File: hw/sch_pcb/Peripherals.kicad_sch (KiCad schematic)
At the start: 50 parts

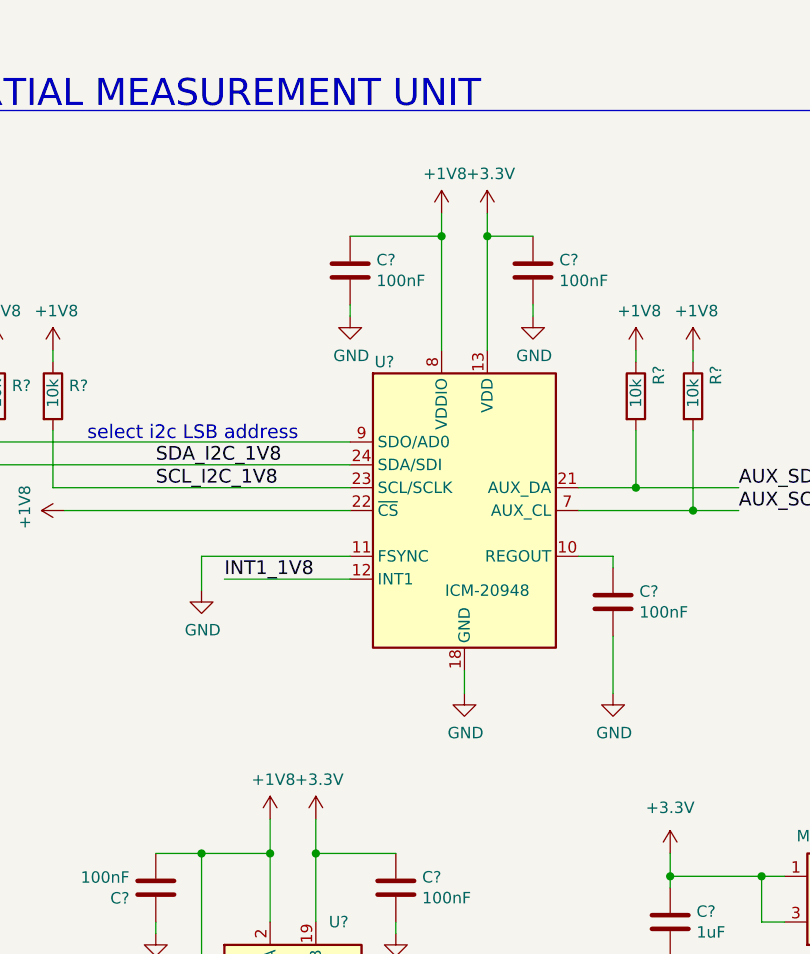
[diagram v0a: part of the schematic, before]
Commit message: Removing Li-ion accumulator BMS Adding ISM02B LoRa telemetry block.
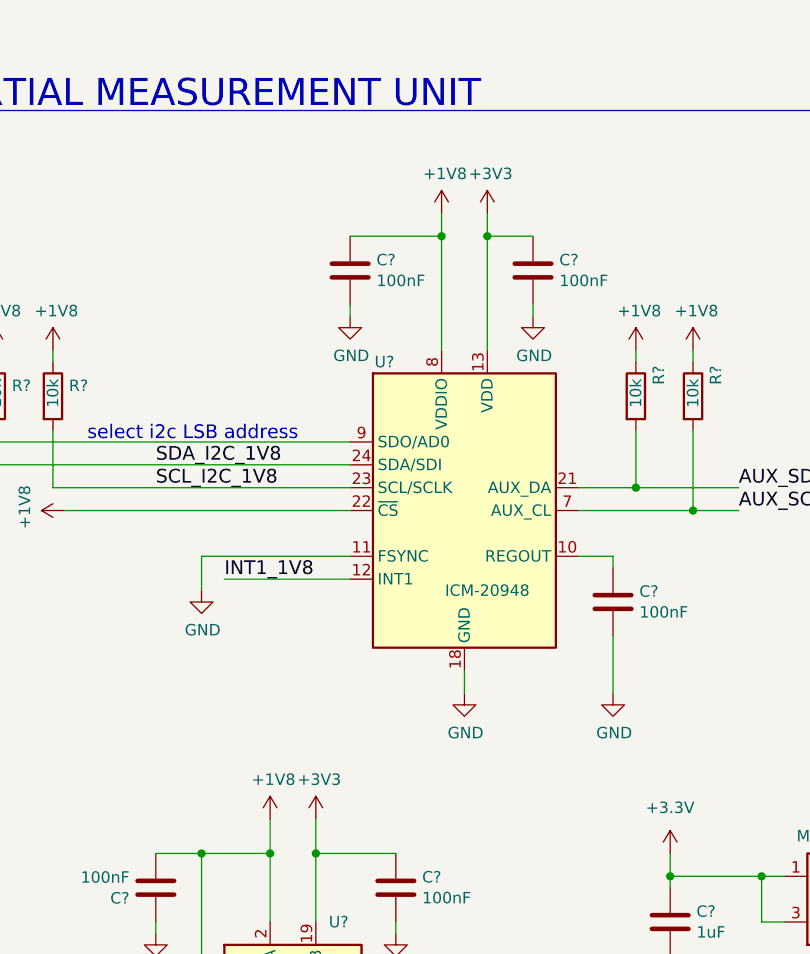
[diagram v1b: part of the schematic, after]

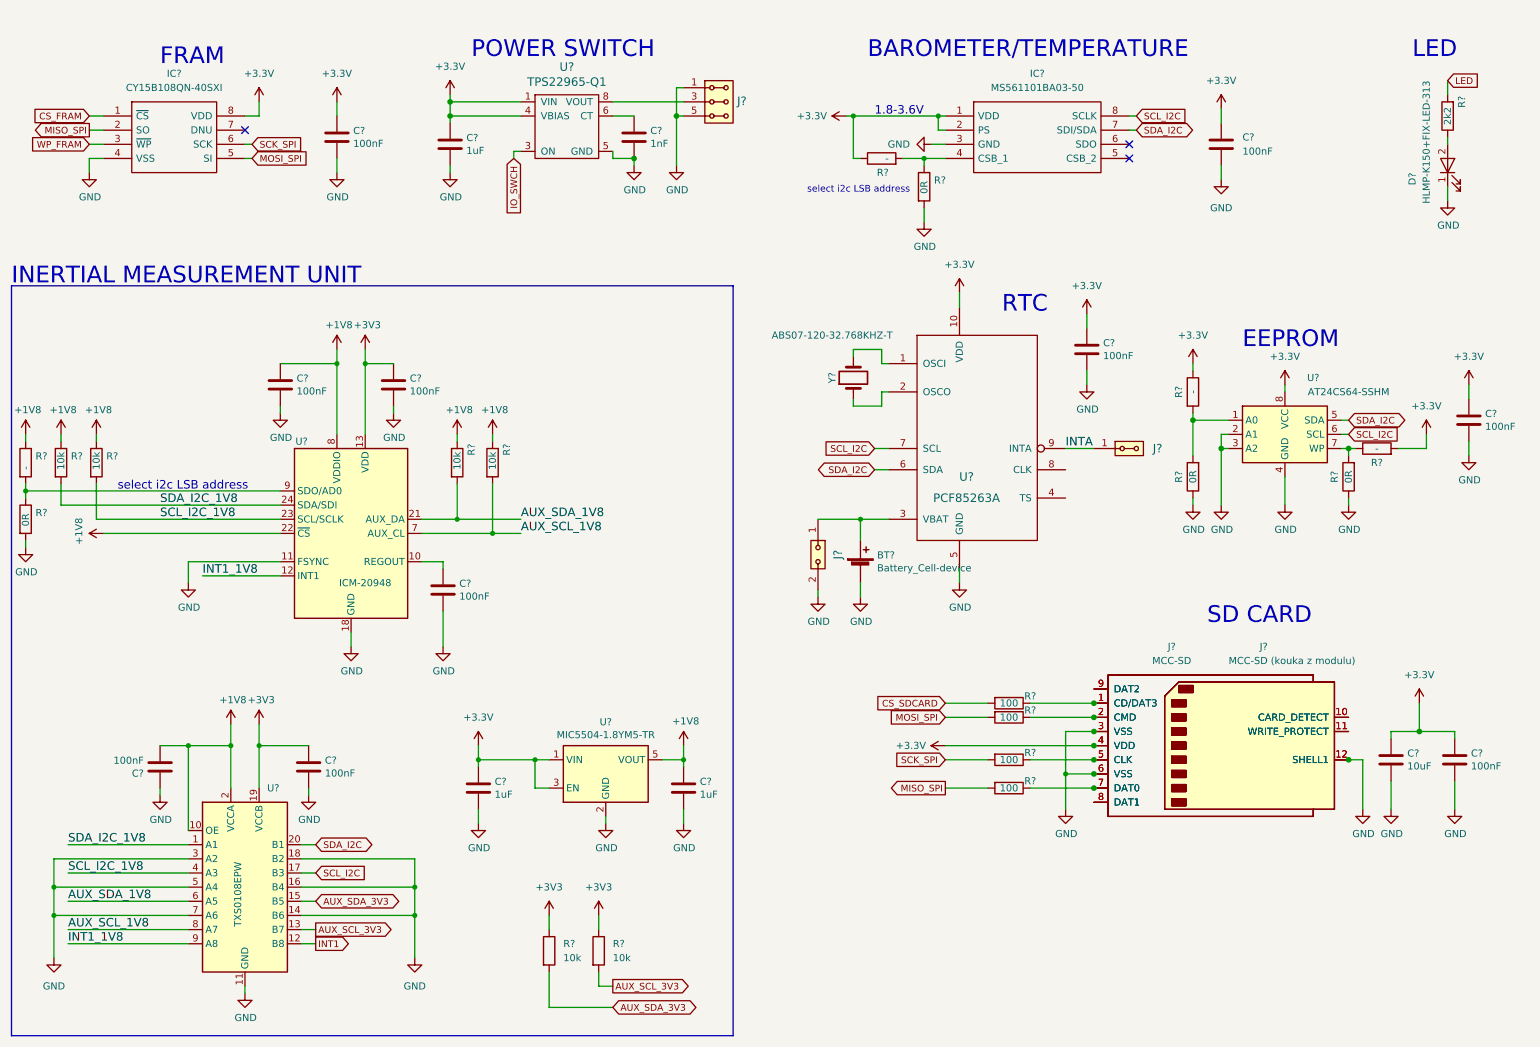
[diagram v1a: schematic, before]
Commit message: schematics update
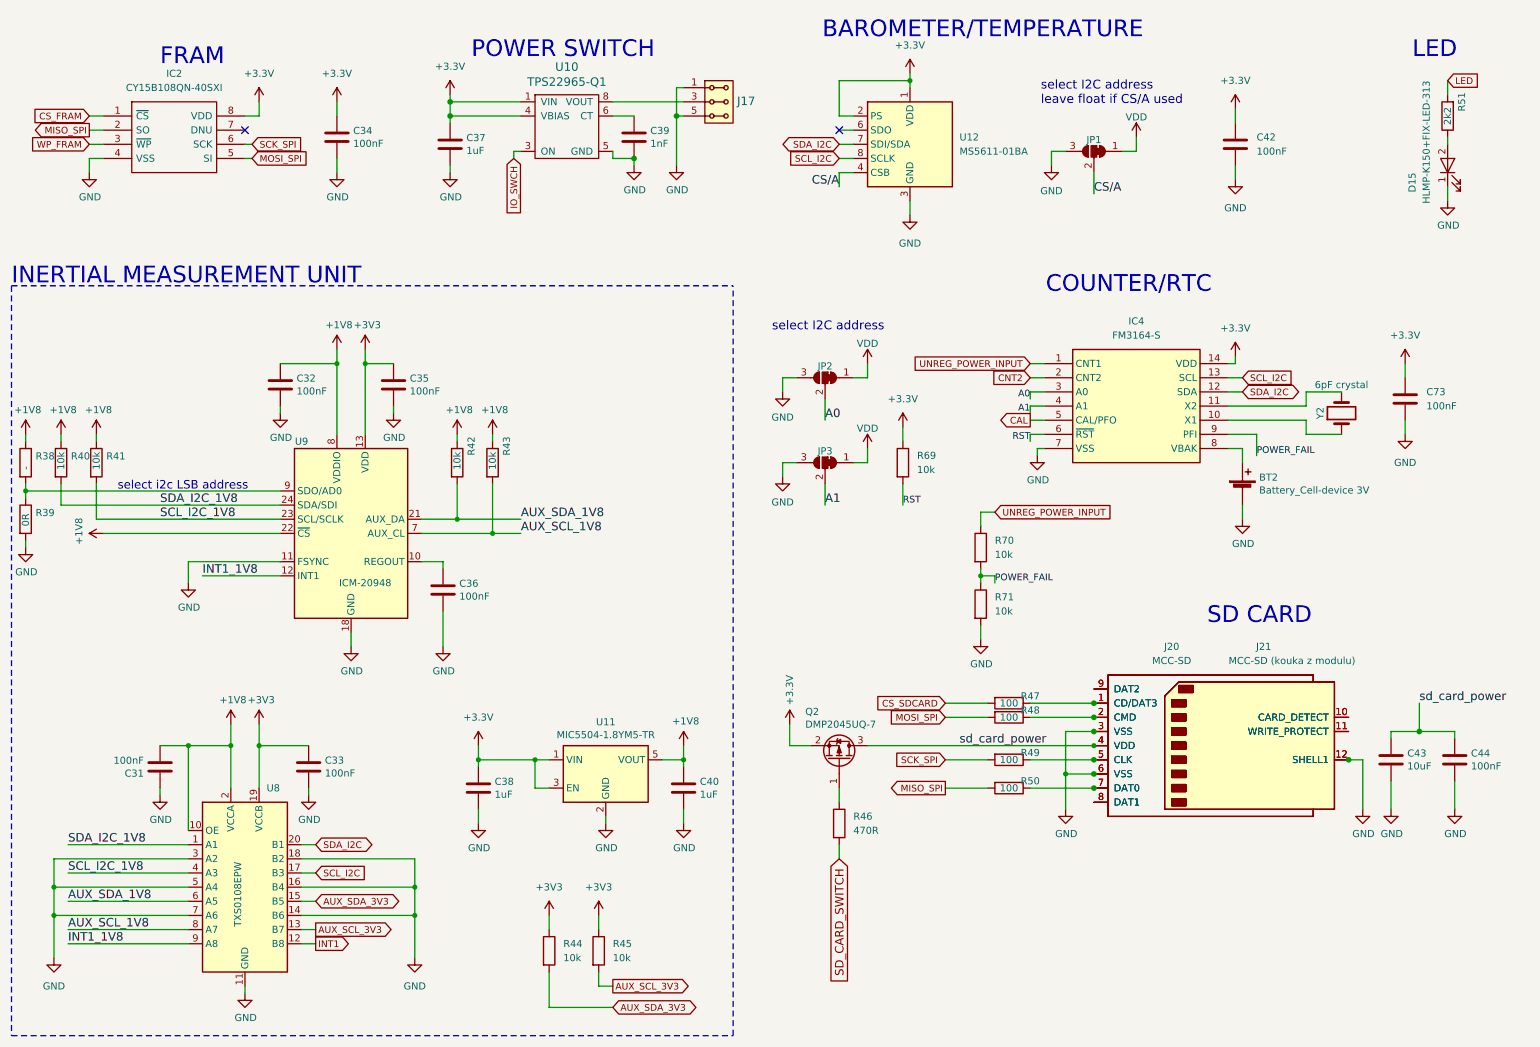
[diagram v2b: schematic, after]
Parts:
- removed C? (x2): 100nF, Mlab_R:SMD-0805, symbol DATALOGGER01A-rescue:C-device
- removed IC?: MS561101BA03-50, MS561101BA03-50, symbol MS561101BA03-50:MS561101BA03-50
- removed J?: HEADER_2x01, Mlab_Pin_Headers:Straight_2x01, symbol DATALOGGER01A-rescue:HEADER_2x01-MLAB_HEADER
- removed J?: HEADER_2x01_PARALLEL, Mlab_Pin_Headers:Straight_2x01, symbol DATALOGGER01A-rescue:HEADER_2x01_PARALLEL-MLAB_HEADER
- removed R? (x2): -, Mlab_R:SMD-0805, symbol DATALOGGER01A-rescue:R-device
- removed R?: -, Mlab_R:SMD-0603, symbol Device:R
- removed R? (x2): 0R, Mlab_R:SMD-0805, symbol DATALOGGER01A-rescue:R-device
- removed R?: 0R, Mlab_R:SMD-0603, symbol Device:R
- removed U?: PCF85263A, Mlab_IO:TSSOP-10_3x3mm_Pitch0.5mm, symbol DATALOGGER01A-rescue:PCF85263A-MLAB_IO
- removed U?: AT24CS64-SSHM, Package_SO:SOIC-8_3.9x4.9mm_P1.27mm, symbol Memory_EEPROM:AT24CS64-SSHM
- added C73: 100nF, symbol Device:C
- added IC4: FM3164-S, SOIC127P600X175-14N, symbol FM3164-S:FM3164-S
- added JP1, JP2, JP3: SolderJumper_3_Bridged12, Jumper:SolderJumper-3_P1.3mm_Bridged12_RoundedPad1.0x1.5mm_NumberLabels, symbol Jumper:SolderJumper_3_Bridged12
- added Q2: DMP2045UQ-7, Package_TO_SOT_SMD:SOT-23, symbol Transistor_FET:IRLML6401
- added R46: 470R, symbol Device:R
- added R69, R70, R71: 10k, symbol Device:R
- added U12: MS5611-01BA, Package_LGA:LGA-8_3x5mm_P1.25mm, symbol Sensor_Pressure:MS5611-01BA
- BT2: renamed from BT?; value Battery_Cell-device -> Battery_Cell-device 3V
- Y2: renamed from Y?; value ABS07-120-32.768KHZ-T -> 6pF crystal
- gave numbers to parts that had none: 35
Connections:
- net +3.3V: now also C73.1, IC4.14 (VDD), Q2.2 (S), R69.1, U12.1 (VDD), U12.2 (PS); no longer C43.1, C44.1, J20.4 (VDD), J21.4 (VDD)
- net GND: now also C73.2, IC4.7 (VSS), JP1.3 (B), JP2.3 (B), JP3.3 (B), R71.2, U12.3 (GND)
- net SCL_I2C: now also IC4.13 (SCL), U12.8 (SCLK)
- net SDA_I2C: now also IC4.12 (SDA), U12.7 (SDI/SDA)
- net at BT2.1 (+): now also IC4.8 (VBAK)
- net at Y2.2: now also IC4.11 (X2)
- net at Y2.1: now also IC4.10 (X1)
- new net: Q2.1 (G), R46.1
- new net A0: IC4.3 (A0), JP2.2 (C)
- new net A1: IC4.4 (A1), JP3.2 (C)
- new net CAL: IC4.5 (CAL/PFO)
- new net CNT2: IC4.2 (CNT2)
- new net CS/A: JP1.2 (C), U12.4 (CSB), U12.5 (CSB)
- new net POWER_FAIL: IC4.9 (PFI), R70.2, R71.1
- new net RST: IC4.6 (~{RST}), R69.2
- new net SD_CARD_SWITCH: R46.2
- new net UNREG_POWER_INPUT: IC4.1 (CNT1), R70.1
- new net VDD: JP1.1 (A), JP2.1 (A), JP3.1 (A)
- new net sd_card_power: C43.1, C44.1, J20.4 (VDD), J21.4 (VDD), Q2.3 (D)
- no-connect marks 3 -> 2
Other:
- note added: "COUNTER/RTC"
- note added: "select I2C address"
- note added: "select I2C address leave float if CS/A used"
- note removed: "1.8-3.6V"
- note removed: "EEPROM"
- note removed: "RTC"
- moved on the sheet: BT2, C42, Y2

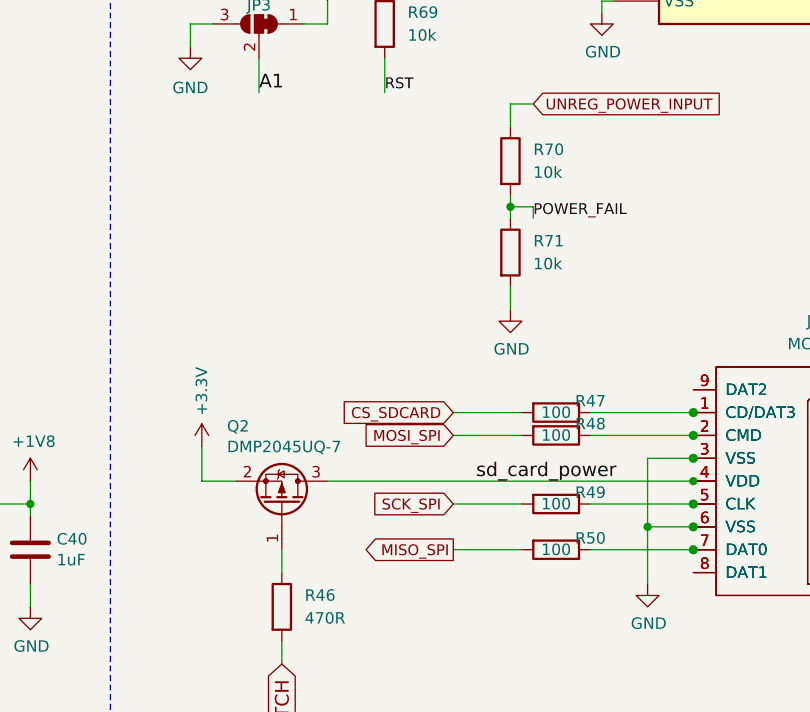
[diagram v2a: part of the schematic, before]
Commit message: schematics update
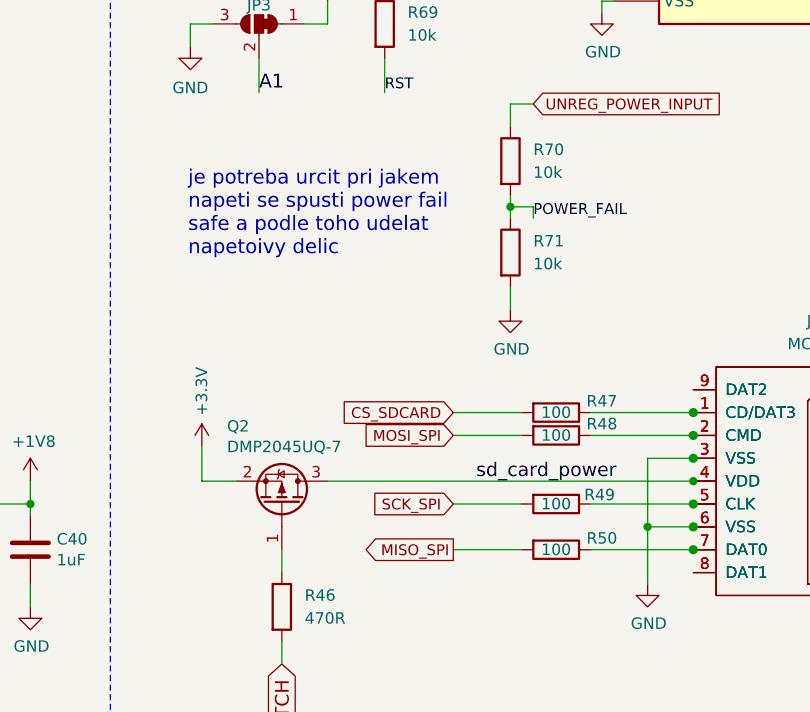
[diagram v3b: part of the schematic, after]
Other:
- note added: "je potreba urcit pri jakem napeti se spusti power fail safe a podle toho udelat napetoivy delic"
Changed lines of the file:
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@@
 		)
 	)
+	(text "je potreba urcit pri jakem\nnapeti se spusti power fail\nsafe a podle toho udelat\nnapetoivy delic"
+		(exclude_from_sim no)
+		(at 152.146 119.888 0)
+		(effects
+			(font
+				(size 1.6 1.6)
+			)
+			(justify left bottom)
+		)
+	)
 	(text "INERTIAL MEASUREMENT UNIT"
 		(exclude_from_sim no)
@@
 		(dnp no)
 		(property "Reference" "R47"
-			(at 196.85 135.89 90)
+			(at 198.12 135.89 90)
 			(effects
 				(font
@@
 		(dnp no)
 		(property "Reference" "R48"
-			(at 196.85 138.43 90)
+			(at 198.12 138.43 90)
 			(effects
 				(font
@@
 		(dnp no)
 		(property "Reference" "R49"
-			(at 196.85 146.05 90)
+			(at 197.866 146.304 90)
 			(effects
 				(font
@@
 		(dnp no)
 		(property "Reference" "R50"
-			(at 196.85 151.13 90)
+			(at 198.12 151.13 90)
 			(effects
 				(font

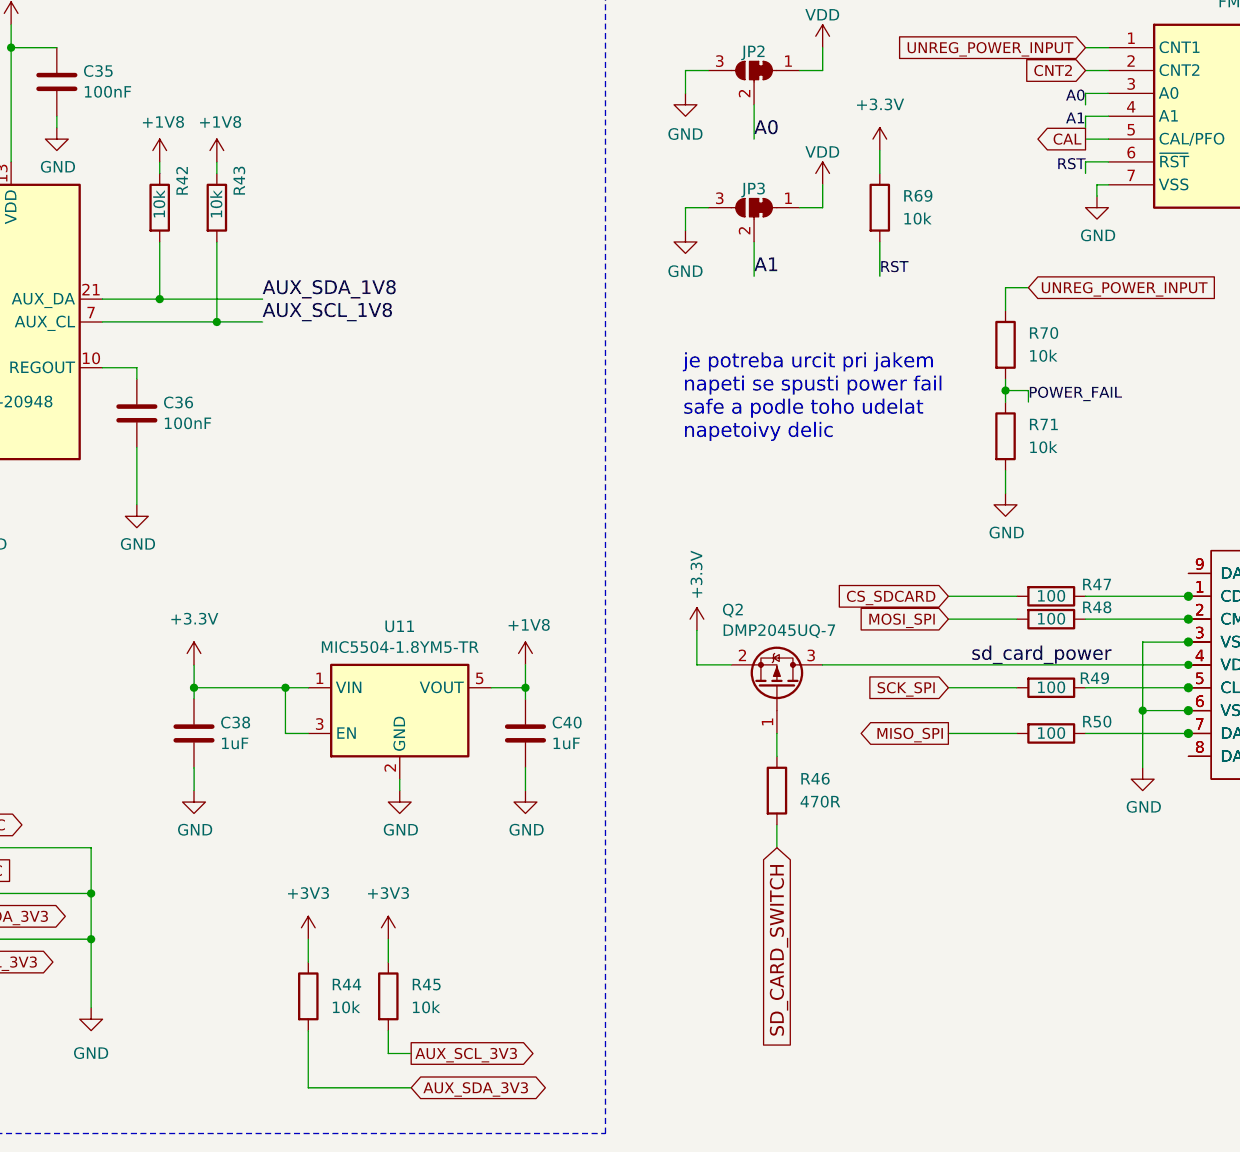
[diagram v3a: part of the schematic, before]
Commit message: schematics update
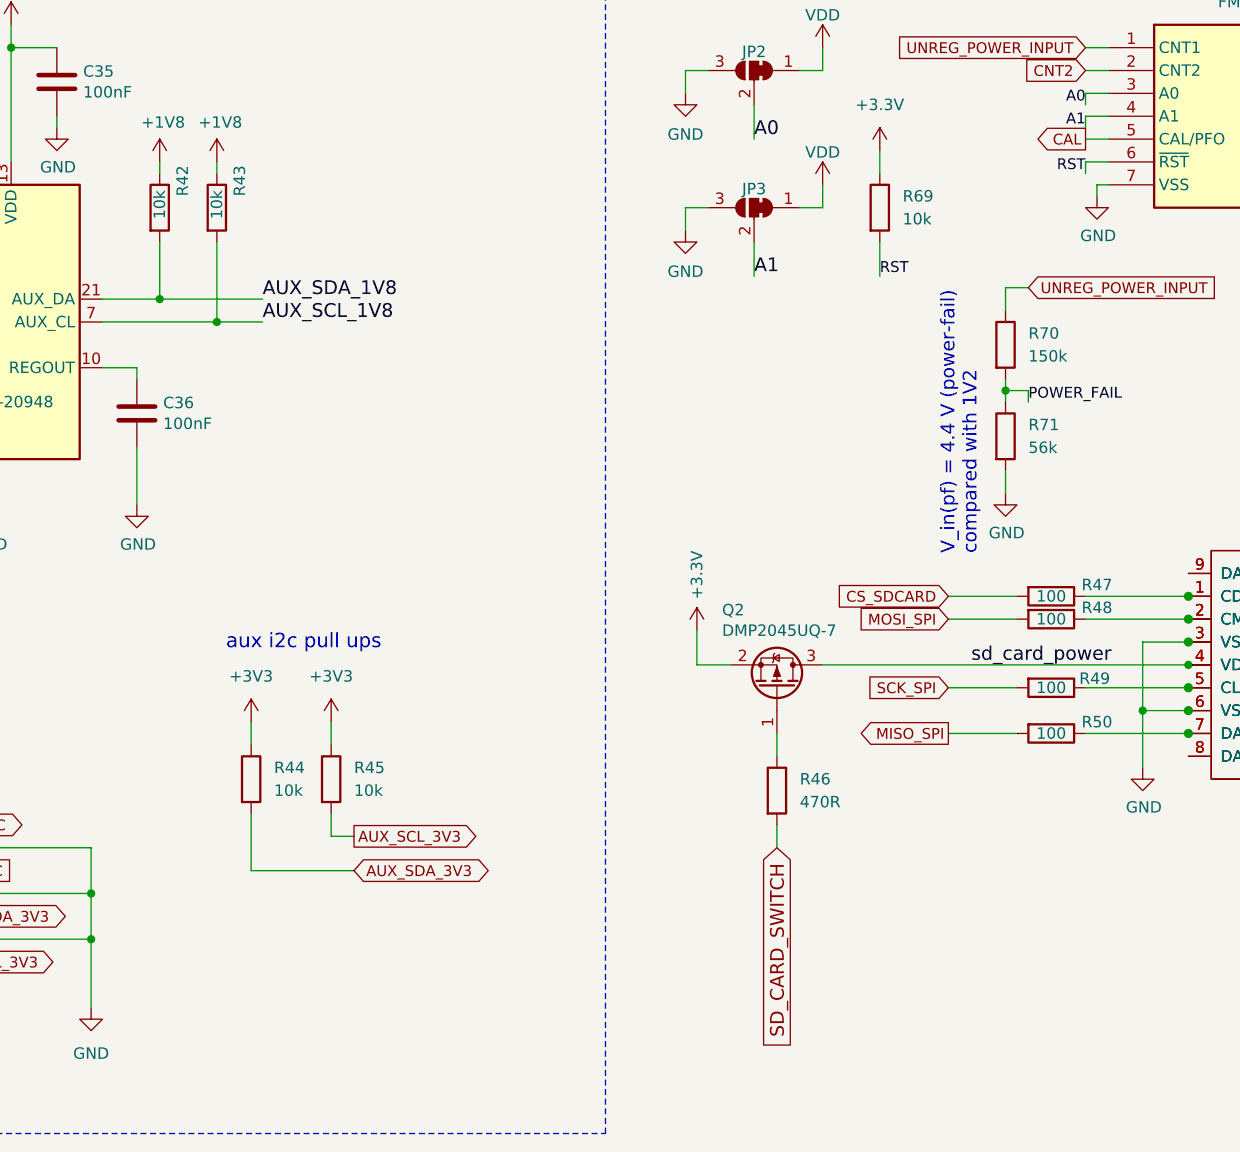
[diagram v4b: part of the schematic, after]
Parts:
- removed C38, C40: 1uF, Mlab_R:SMD-0603, symbol Device:C
- removed U11: MIC5504-1.8YM5-TR, Package_TO_SOT_SMD:SOT-23-5, symbol Regulator_Linear:MIC5504-1.8YM5
- R70: value 10k -> 150k
- R71: value 10k -> 56k
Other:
- note added: "V_in(pf) = 4.4 V (power-fail) compared with 1V2"
- note added: "aux i2c pull ups"
- note removed: "je potreba urcit pri jakem napeti se spusti power fail safe a podle toho udelat napetoivy delic"
- moved on the sheet: R44, R45
